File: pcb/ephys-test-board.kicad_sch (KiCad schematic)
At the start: 4 parts, among them J1 Conn_02x10_Odd_Even, J8 BM03B-SRSS-TB

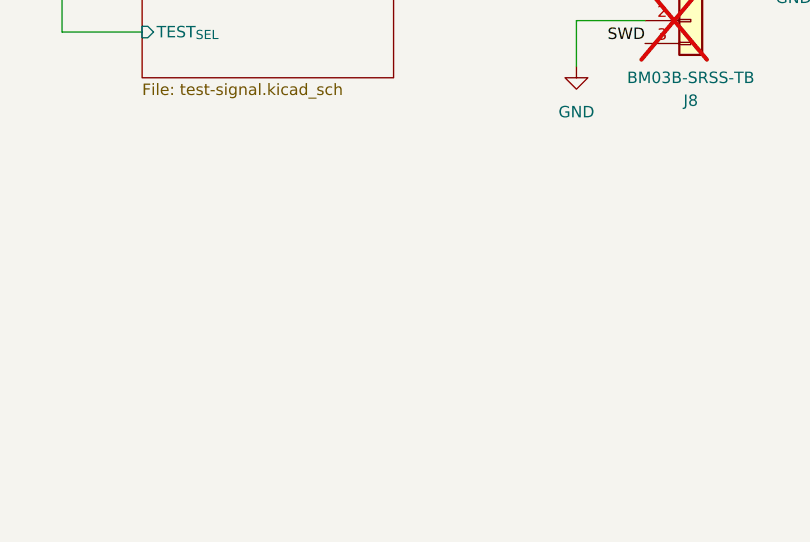
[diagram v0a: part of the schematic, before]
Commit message: Start routing rev. A
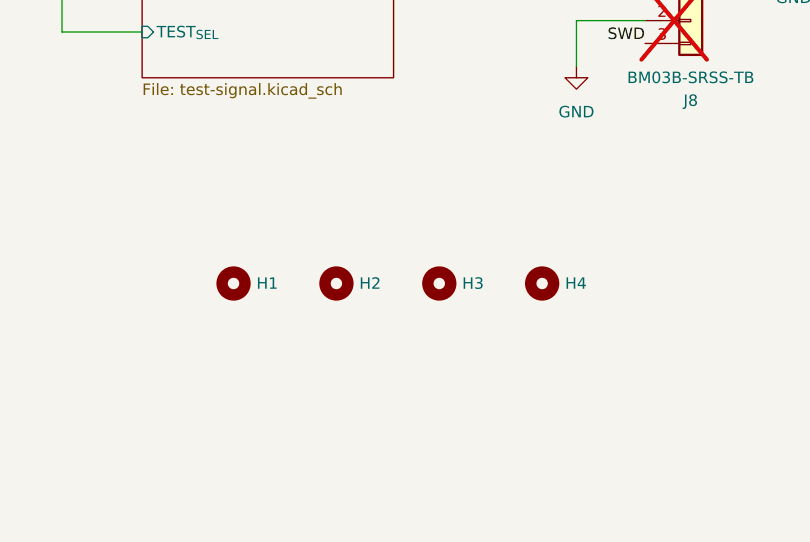
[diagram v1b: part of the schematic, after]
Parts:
- added H1, H2, H3, H4: ~, MountingHole:MountingHole_3.2mm_M3_ISO7380_Pad, symbol Mechanical:MountingHole
- J1: footprint Connector_PinSocket_2.54mm:PinSocket_2x10_P2.54mm_Vertical -> Connector_PinHeader_2.54mm:PinHeader_2x10_P2.54mm_Vertical

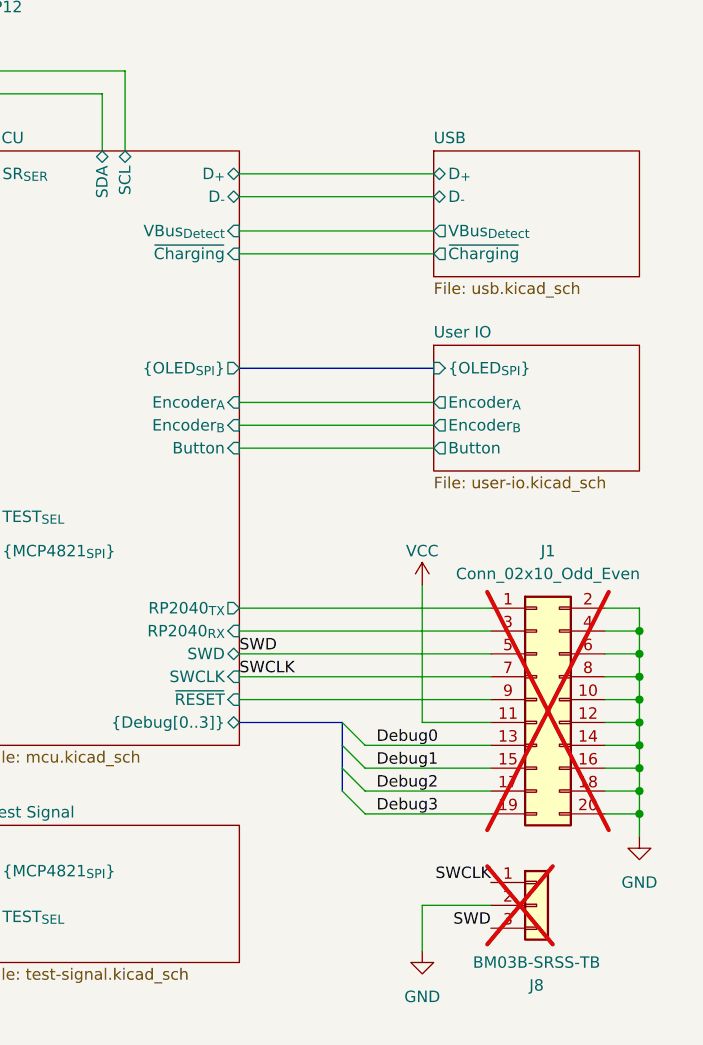
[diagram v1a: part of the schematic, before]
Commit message: Routing nearly complete
- Power switch is too tall I think
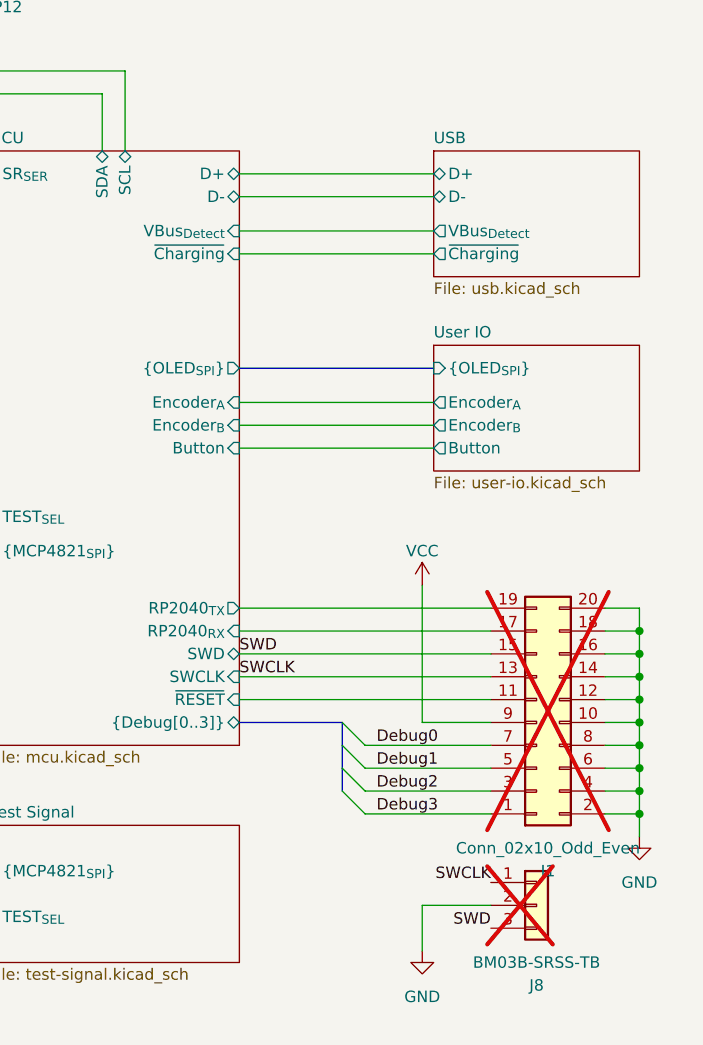
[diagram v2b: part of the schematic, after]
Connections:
- net Debug0: now also J1.7 (Pin_7); no longer J1.13 (Pin_13)
- net Debug1: now also J1.5 (Pin_5); no longer J1.15 (Pin_15)
- net Debug2: now also J1.3 (Pin_3); no longer J1.17 (Pin_17)
- net Debug3: now also J1.1 (Pin_1); no longer J1.19 (Pin_19)
- net MCU/RP2040_{RX}: now also J1.17 (Pin_17); no longer J1.3 (Pin_3)
- net MCU/RP2040_{TX}: now also J1.19 (Pin_19); no longer J1.1 (Pin_1)
- net MCU/~{RESET}: now also J1.11 (Pin_11); no longer J1.9 (Pin_9)
- net SWCLK: now also J1.13 (Pin_13); no longer J1.7 (Pin_7)
- net SWD: now also J1.15 (Pin_15); no longer J1.5 (Pin_5)
- net VCC: now also J1.9 (Pin_9); no longer J1.11 (Pin_11)
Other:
- sheet MCU ports: added D+, D-; removed D_{+}, D_{-}
- sheet USB ports: added D+, D-; removed D_{+}, D_{-}
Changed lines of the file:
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@@
+			)
+		)
+		(property "Voltage" ""
+			(at 236.22 151.13 0)
+			(effects
+				(font
+					(size 1.27 1.27)
+				)
+				(hide yes)
 			)
 		)
@@
 		)
 		(property "Description" "Mounting Hole without connection"
+			(at 201.93 151.13 0)
+			(effects
+				(font
+					(size 1.27 1.27)
+				)
+				(hide yes)
+			)
+		)
+		(property "Voltage" ""
 			(at 201.93 151.13 0)
 			(effects
@@
 	(symbol
 		(lib_id "Connector_Generic:Conn_02x10_Odd_Even")
-		(at 252.73 99.06 0)
+		(at 252.73 101.6 0)
+		(mirror x)
 		(unit 1)
 		(exclude_from_sim no)
@@
 		(on_board yes)
 		(dnp yes)
-		(fields_autoplaced yes)
 		(property "Reference" "J1"
-			(at 254 82.55 0)
+			(at 254 118.11 0)
 			(effects
 				(font
@@
 		)
 		(property "Value" "Conn_02x10_Odd_Even"
-			(at 254 85.09 0)
+			(at 254 115.57 0)
 			(effects
 				(font
@@
 		)
 		(property "Footprint" "Connector_PinHeader_2.54mm:PinHeader_2x10_P2.54mm_Vertical"
-			(at 252.73 99.06 0)
+			(at 252.73 101.6 0)
 			(effects
 				(font
@@
 		)
 		(property "Datasheet" "~"
-			(at 252.73 99.06 0)
+			(at 252.73 101.6 0)
 			(effects
 				(font
@@
 		)
 		(property "Description" "Generic connector, double row, 02x10, odd/even pin numbering scheme (row 1 odd numbers, row 2 even numbers), script generated (kicad-library-utils/schlib/autogen/connector/)"
-			(at 252.73 99.06 0)
+			(at 252.73 101.6 0)
+			(effects
+				(font
+					(size 1.27 1.27)
+				)
+				(hide yes)
+			)
+		)
+		(property "Voltage" ""
+			(at 252.73 101.6 0)
 			(effects
 				(font
@@
 		)
 		(property "Description" "Mounting Hole without connection"
+			(at 213.36 151.13 0)
+			(effects
+				(font
+					(size 1.27 1.27)
+				)
+				(hide yes)
+			)
+		)
+		(property "Voltage" ""
 			(at 213.36 151.13 0)
 			(effects
@@
 			)
 		)
+		(property "Voltage" ""
+			(at 252.73 121.92 0)
+			(effects
+				(font
+					(size 1.27 1.27)
+				)
+				(hide yes)
+			)
+		)
 		(pin "2"
 		)
@@
 			)
 		)
+		(property "Voltage" ""
+			(at 190.5 26.67 0)
+			(effects
+				(font
+					(size 1.27 1.27)
+				)
+				(hide yes)
+			)
+		)
 		(pin "1"
 		)
@@
 		)
 		(property "Description" "Mounting Hole without connection"
+			(at 224.79 151.13 0)
+			(effects
+				(font
+					(size 1.27 1.27)
+				)
+				(hide yes)
+			)
+		)
+		(property "Voltage" ""
 			(at 224.79 151.13 0)
 			(effects
@@
 			)
 		)
+		(property "Voltage" ""
+			(at 182.88 26.67 0)
+			(effects
+				(font
+					(size 1.27 1.27)
+				)
+				(hide yes)
+			)
+		)
 		(pin "1"
 		)
@@
 			)
 		)
-		(pin "D_{-}" bidirectional
+		(pin "D-" bidirectional
 			(at 241.3 43.18 180)
 			(effects
@@
 			)
 		)
-		(pin "D_{+}" bidirectional
+		(pin "D+" bidirectional
 			(at 241.3 40.64 180)
 			(effects
@@
 			)
 		)
-		(pin "D_{-}" bidirectional
+		(pin "D-" bidirectional
 			(at 219.71 43.18 0)
 			(effects
@@
 			)
 		)
-		(pin "D_{+}" bidirectional
+		(pin "D+" bidirectional
 			(at 219.71 40.64 0)
 			(effects

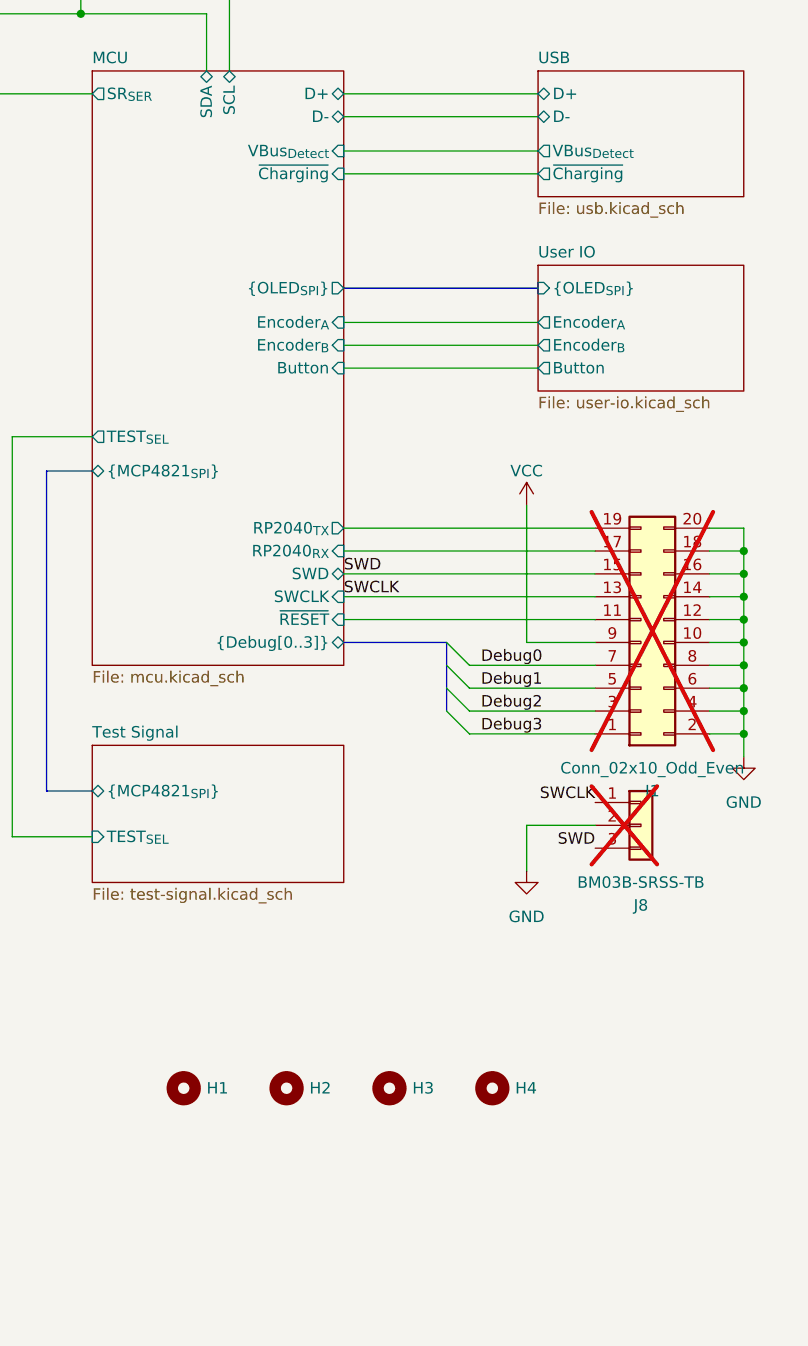
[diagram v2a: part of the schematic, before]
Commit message: Rev. A of PCB
- I will make a case before fabrication so that they can be made
  together
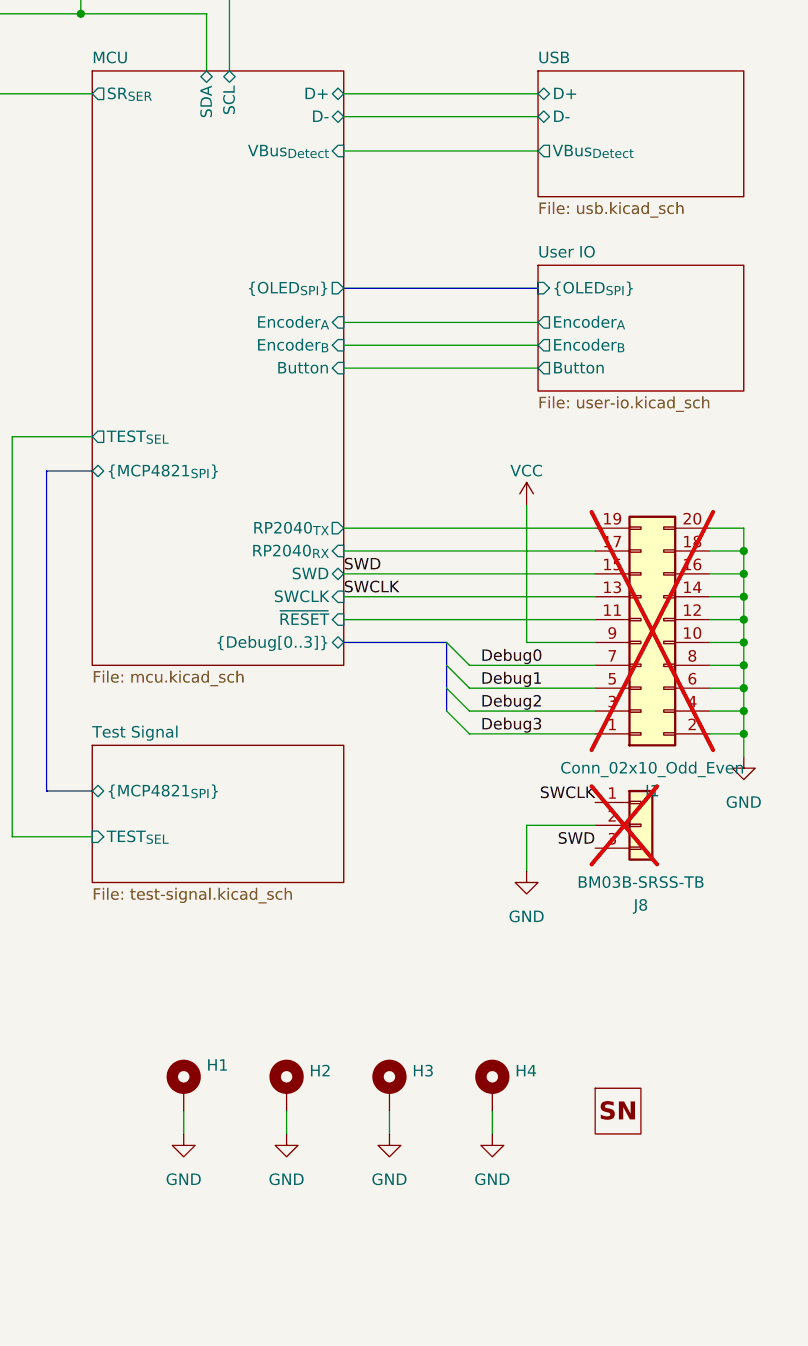
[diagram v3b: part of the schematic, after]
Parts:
- added H5: ~, open-ephys:OEPS_SN-STICKER-8x20mm, symbol open-ephys:OEPS-SN
- H1, H2, H3, H4: symbol Mechanical:MountingHole -> Mechanical:MountingHole_Pad
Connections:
- net GND: now also H1.1, H2.1, H3.1, H4.1
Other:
- sheet MCU ports: added none; removed ~{Charging}
- sheet USB ports: added none; removed ~{Charging}

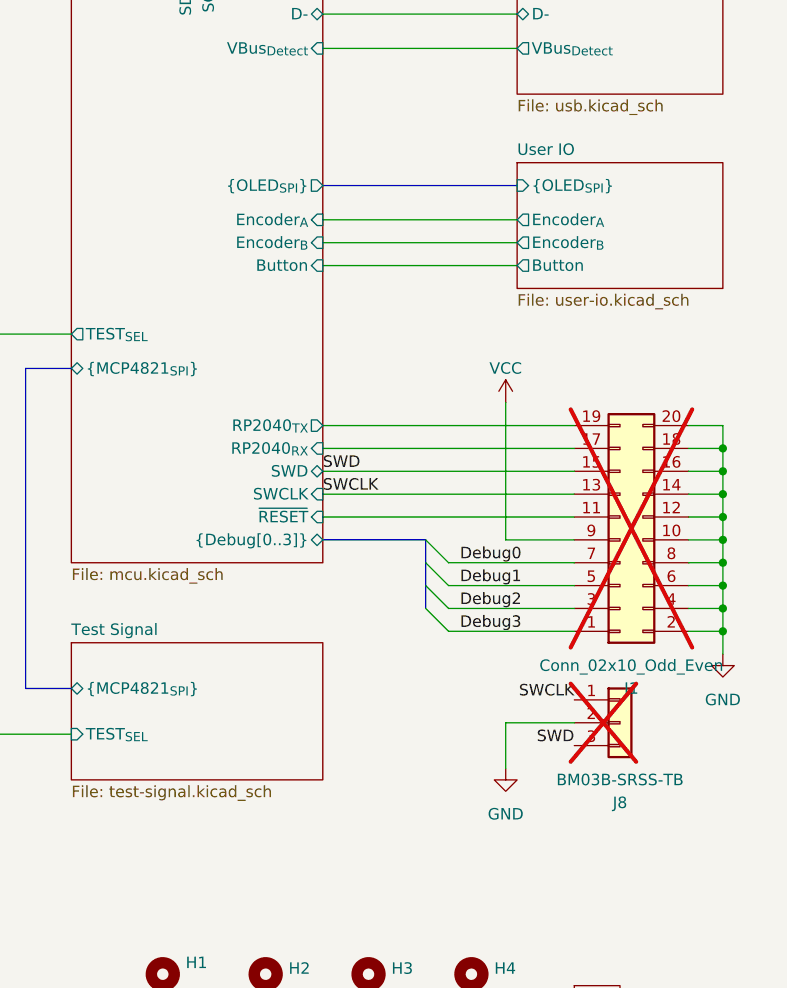
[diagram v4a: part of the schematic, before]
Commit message: Address several issues found when testing rev. A
- Add Reset button to back panel
- Make board smaller
- Move battery to bottom of device
- Replace OLED with a more reasonable choice.
- Etc.
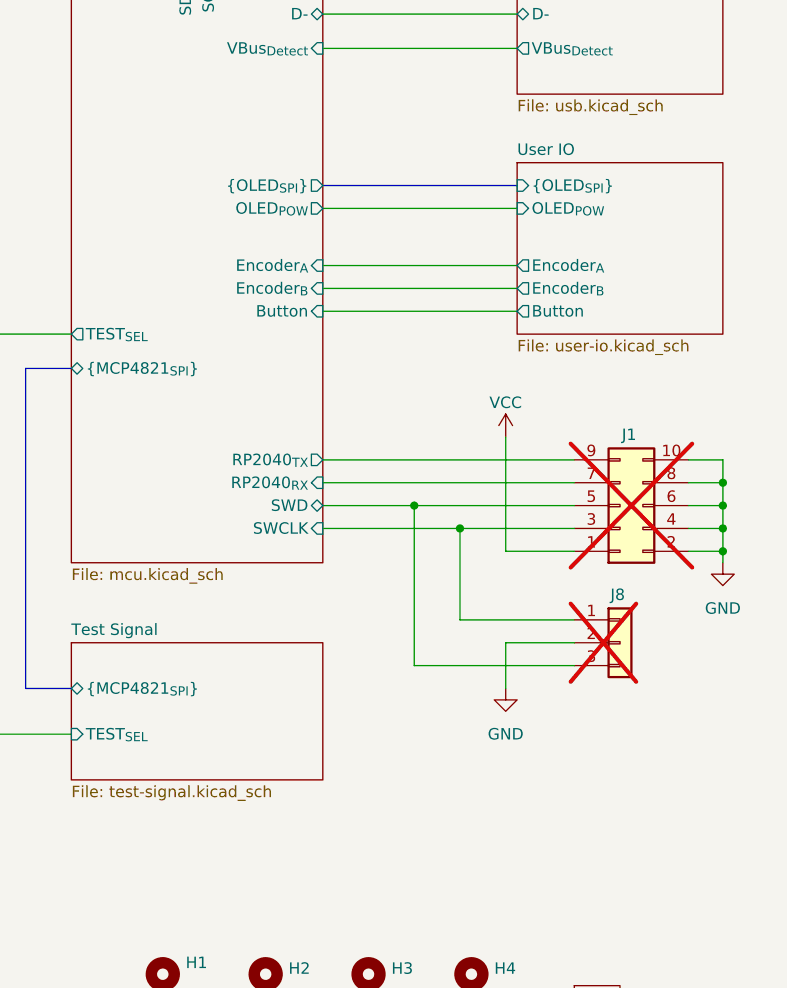
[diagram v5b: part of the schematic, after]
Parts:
- removed J1: Conn_02x10_Odd_Even, Connector_PinHeader_2.54mm:PinHeader_2x10_P2.54mm_Vertical, symbol Connector_Generic:Conn_02x10_Odd_Even
- added J1: Conn_02x10_Odd_Even, Connector_PinHeader_2.54mm:PinHeader_2x05_P2.54mm_Vertical_SMD, symbol Connector_Generic:Conn_02x05_Odd_Even
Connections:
- net GND: now also J1.10 (Pin_10), J1.2 (Pin_2), J1.4 (Pin_4), J1.6 (Pin_6), J1.8 (Pin_8)
- net MCU/RP2040_{RX}: now also J1.7 (Pin_7)
- net MCU/RP2040_{TX}: now also J1.9 (Pin_9)
- net VCC: now also J1.1 (Pin_1)
- net SWCLK renamed MCU/SWCLK
- net MCU/SWCLK: now also J1.3 (Pin_3)
- net SWD renamed MCU/SWD
- net MCU/SWD: now also J1.5 (Pin_5)
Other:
- sheet MCU ports: added OLED_{POW}; removed {Debug[0..3]}, ~{RESET}
- sheet User IO ports: added OLED_{POW}; removed none
- moved on the sheet: J8
